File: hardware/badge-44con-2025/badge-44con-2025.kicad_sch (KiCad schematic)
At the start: 28 parts, among them J1 128x64 OLED Display, J2 Conn_02x03_Odd_Even, SW1 RESET, SW2 SW_Nidec_CAS-120A1, U1 ESP32-WEMOS D1 mini, U2 CH32V003FxPx, U3 MT3608_Boost_converter, U4 AD8317_Module

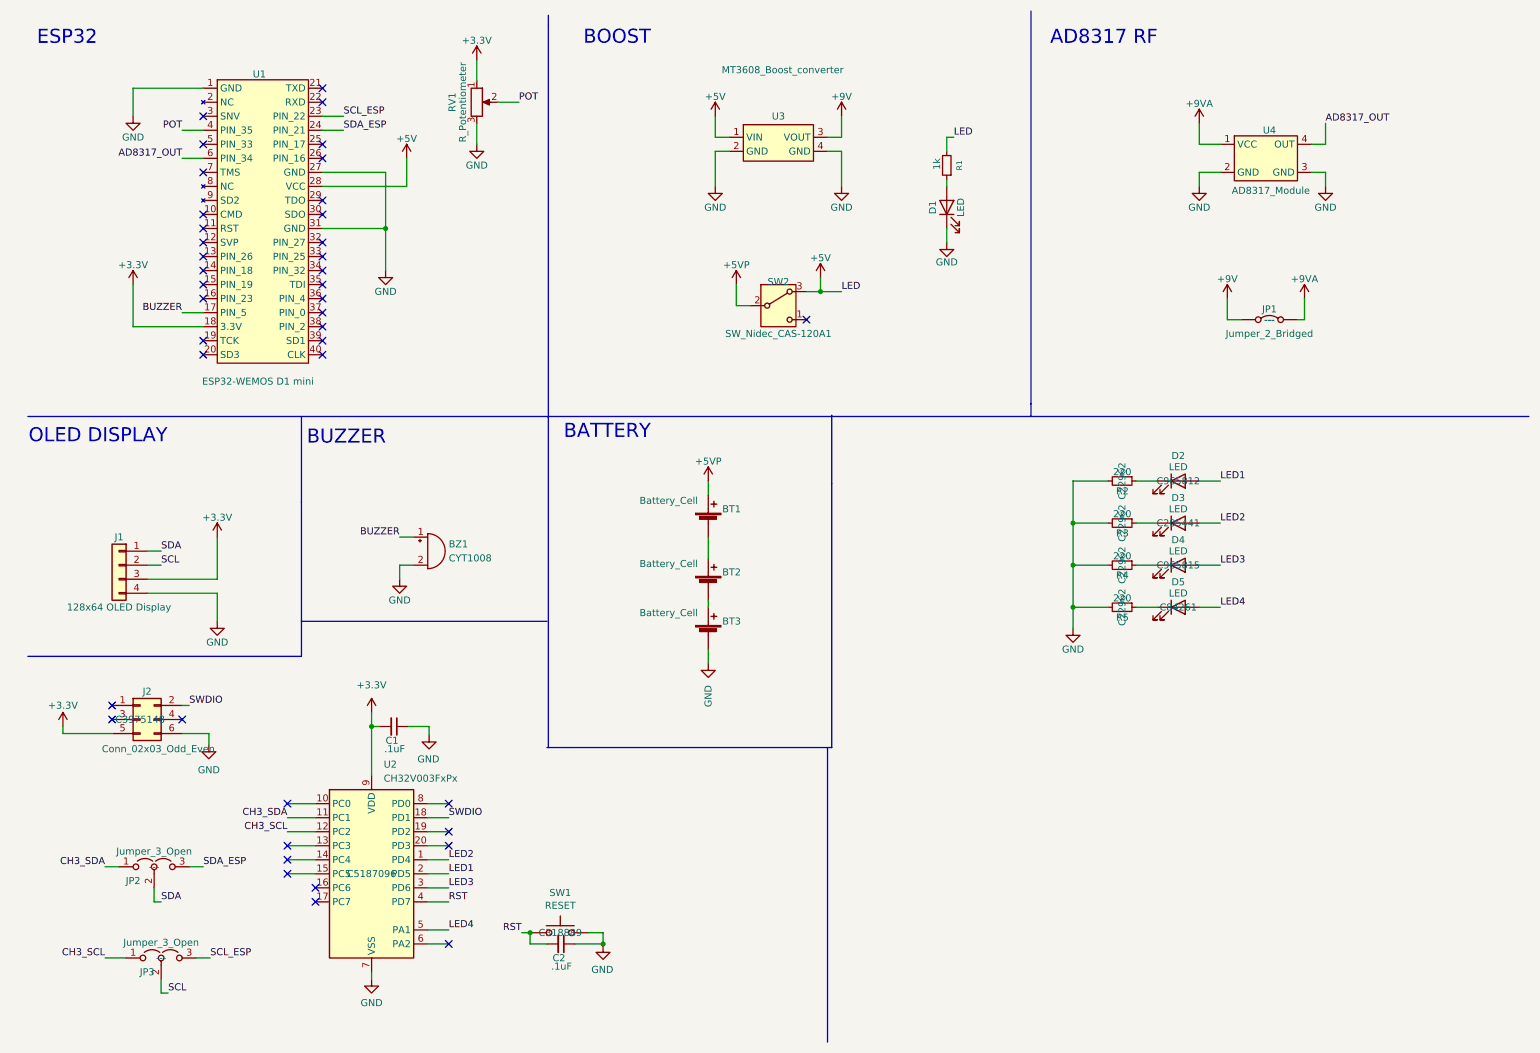
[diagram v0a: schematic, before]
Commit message: feat(Hw):Added_buttons
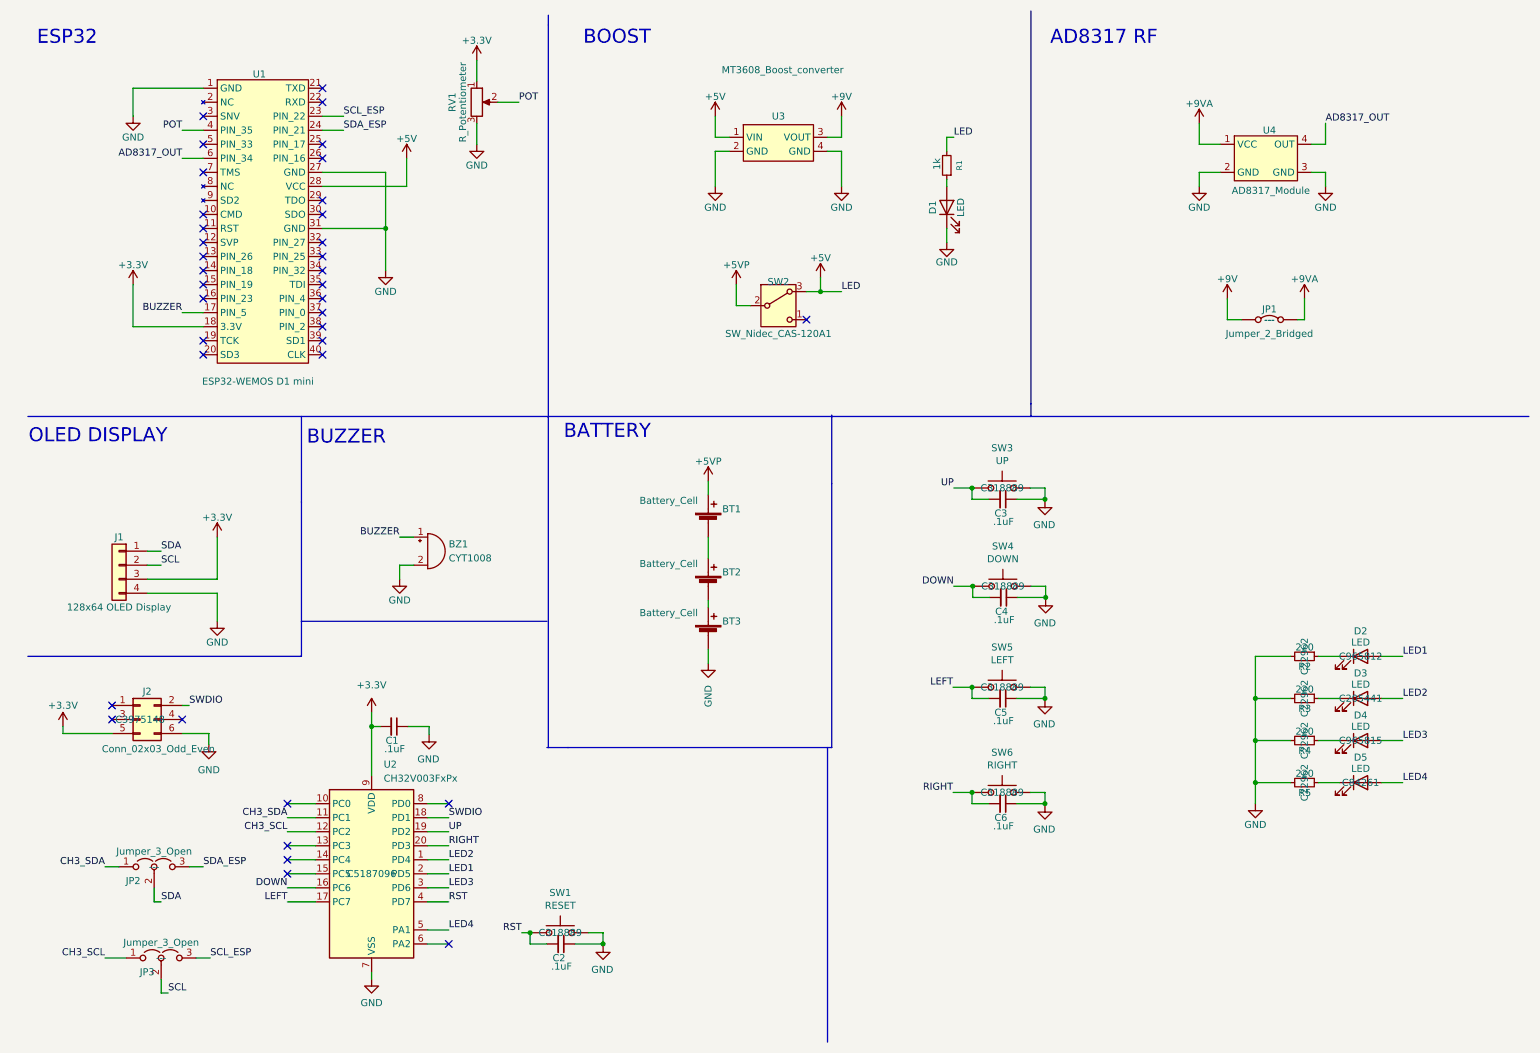
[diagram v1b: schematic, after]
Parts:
- added C3, C4, C5, C6: .1uF, Capacitor_SMD:C_0603_1608Metric, symbol Device:C_Small
- added SW3: UP, Button_Switch_SMD:SW_SPST_TL3342, symbol Switch:SW_Push
- added SW4: DOWN, Button_Switch_SMD:SW_SPST_TL3342, symbol Switch:SW_Push
- added SW5: LEFT, Button_Switch_SMD:SW_SPST_TL3342, symbol Switch:SW_Push
- added SW6: RIGHT, Button_Switch_SMD:SW_SPST_TL3342, symbol Switch:SW_Push
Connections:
- net GND: now also C3.1, C4.1, C5.1, C6.1, SW3.1, SW4.1, SW5.1, SW6.1
- net DOWN: now reaches U2.16 (PC6)
- net DOWN: now also C4.2, SW4.2
- net LEFT: now reaches U2.17 (PC7)
- net LEFT: now also C5.2, SW5.2
- net UP: now reaches U2.19 (PD2)
- net UP: now also C3.2, SW3.2
- net RIGHT: now reaches U2.20 (PD3)
- net RIGHT: now also C6.2, SW6.2
- no-connect marks 41 -> 37
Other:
- moved on the sheet: D2, D3, D4, D5, R2, R3, R4, R5

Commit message: fix(Hw): fixed_leds_BOM
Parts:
- D2: #LCSC C965812 -> C965799; LCSC# C965812 -> C965799
- D3: #LCSC C205441 -> C965807; LCSC# C205441 -> C965807
- D4: #LCSC C965815 -> C965804; LCSC# C965815 -> C965804
- D5: #LCSC C84261 -> C965802; LCSC# C84261 -> C965802
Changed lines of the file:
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@@
 			)
 		)
-		(property "LCSC#" "C84261"
+		(property "LCSC#" "C965802"
 			(at 254 151.13 0)
 			(effects
@@
 			)
 		)
-		(property "#LCSC" "C84261"
+		(property "#LCSC" "C965802"
 			(at 254 151.13 0)
 			(effects
@@
 			)
 		)
-		(property "LCSC#" "C205441"
+		(property "LCSC#" "C965807"
 			(at 254 135.89 0)
 			(effects
@@
 			)
 		)
-		(property "#LCSC" "C205441"
+		(property "#LCSC" "C965807"
 			(at 254 135.89 0)
 			(effects
@@
 			)
 		)
-		(property "LCSC#" "C965815"
+		(property "LCSC#" "C965804"
 			(at 254 143.51 0)
 			(effects
@@
 			)
 		)
-		(property "#LCSC" "C965815"
+		(property "#LCSC" "C965804"
 			(at 254 143.51 0)
 			(effects
@@
 			)
 		)
-		(property "LCSC#" "C965812"
+		(property "LCSC#" "C965799"
 			(at 254 128.27 0)
 			(effects
@@
 			)
 		)
-		(property "#LCSC" "C965812"
+		(property "#LCSC" "C965799"
 			(at 254 128.27 0)
 			(effects

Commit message: Feat(Hw): Updated_BOM
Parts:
- removed C3, C4, C5, C6: .1uF, Capacitor_SMD:C_0603_1608Metric, symbol Device:C_Small
- removed JP2, JP3: Jumper_3_Open, Jumper:SolderJumper-3_P1.3mm_Bridged2Bar12_RoundedPad1.0x1.5mm, symbol Jumper:Jumper_3_Open
- removed SW3: UP, Button_Switch_SMD:SW_SPST_TL3342, symbol Switch:SW_Push
- removed SW4: DOWN, Button_Switch_SMD:SW_SPST_TL3342, symbol Switch:SW_Push
- removed SW5: LEFT, Button_Switch_SMD:SW_SPST_TL3342, symbol Switch:SW_Push
- removed SW6: RIGHT, Button_Switch_SMD:SW_SPST_TL3342, symbol Switch:SW_Push
- BT1, BT2, BT3, C1, C2: provedor (none) -> LCSC
- D1: LCSC# (none) -> C434424
- D2: #LCSC C965799 -> (none); LCSC# C965799 -> C434424; provedor (none) -> LCSC
- D3: #LCSC C965807 -> (none); LCSC# C965807 -> C434424; provedor (none) -> LCSC
- D4: #LCSC C965804 -> (none); LCSC# C965804 -> C434424; provedor (none) -> LCSC
- D5: #LCSC C965802 -> (none); LCSC# C965802 -> C434424; provedor (none) -> LCSC
- J2: #LCSC C3975148 -> (none); provedor (none) -> LCSC
- R1: LCSC# (none) -> C21190
- R2, R3, R4, R5: #LCSC C22962 -> (none); provedor (none) -> LCSC
- SW1: #LCSC C318889 -> (none); provedor (none) -> LCSC
- SW2: footprint badge-44con-2025:JS102011SAQN -> badge-44con-2025:a12013100ux0116; #LCSC C221660 -> (none); manf# (none) -> https://www.amazon.com/gp/product/B007QAJUUS; provedor LCSC -> Amazon
- U2: #LCSC C5187096 -> (none); provedor (none) -> LCSC
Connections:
- net CH3_SCL is gone; now on net SCL: U2.12 (PC2)
- net CH3_SDA is gone; now on net SDA: U2.11 (PC1)
- net RIGHT is gone; now on net LED1: U2.20 (PD3)
- net GND: no longer R2.2, R3.2, R4.2, R5.2
- net LED1: no longer U2.2 (PD5)
- net LED2: now also U2.2 (PD5); no longer U2.1 (PD4)
- net LED3: now also U2.1 (PD4); no longer U2.3 (PD6)
- net SCL: no longer J1.2 (Pin_2)
- net SCL_ESP: now also J1.2 (Pin_2)
- net SDA: no longer J1.1 (Pin_1)
- net SDA_ESP: now also J1.1 (Pin_1)
- net DOWN: no longer names the net of U2.16 (PC6)
- net LEFT: no longer names the net of U2.17 (PC7)
- net UP: no longer names the net of U2.19 (PD2)
- new net: R2.2, R3.2, R4.2, R5.2
- no-connect marks 37 -> 41
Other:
- moved on the sheet: D2, D3, D4, D5, J2, R2, R3, R4, R5
